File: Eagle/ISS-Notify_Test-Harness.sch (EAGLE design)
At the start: 36 parts, among them U1 ATMEGA32U4, U3 TPS63001, X1 8 MHz

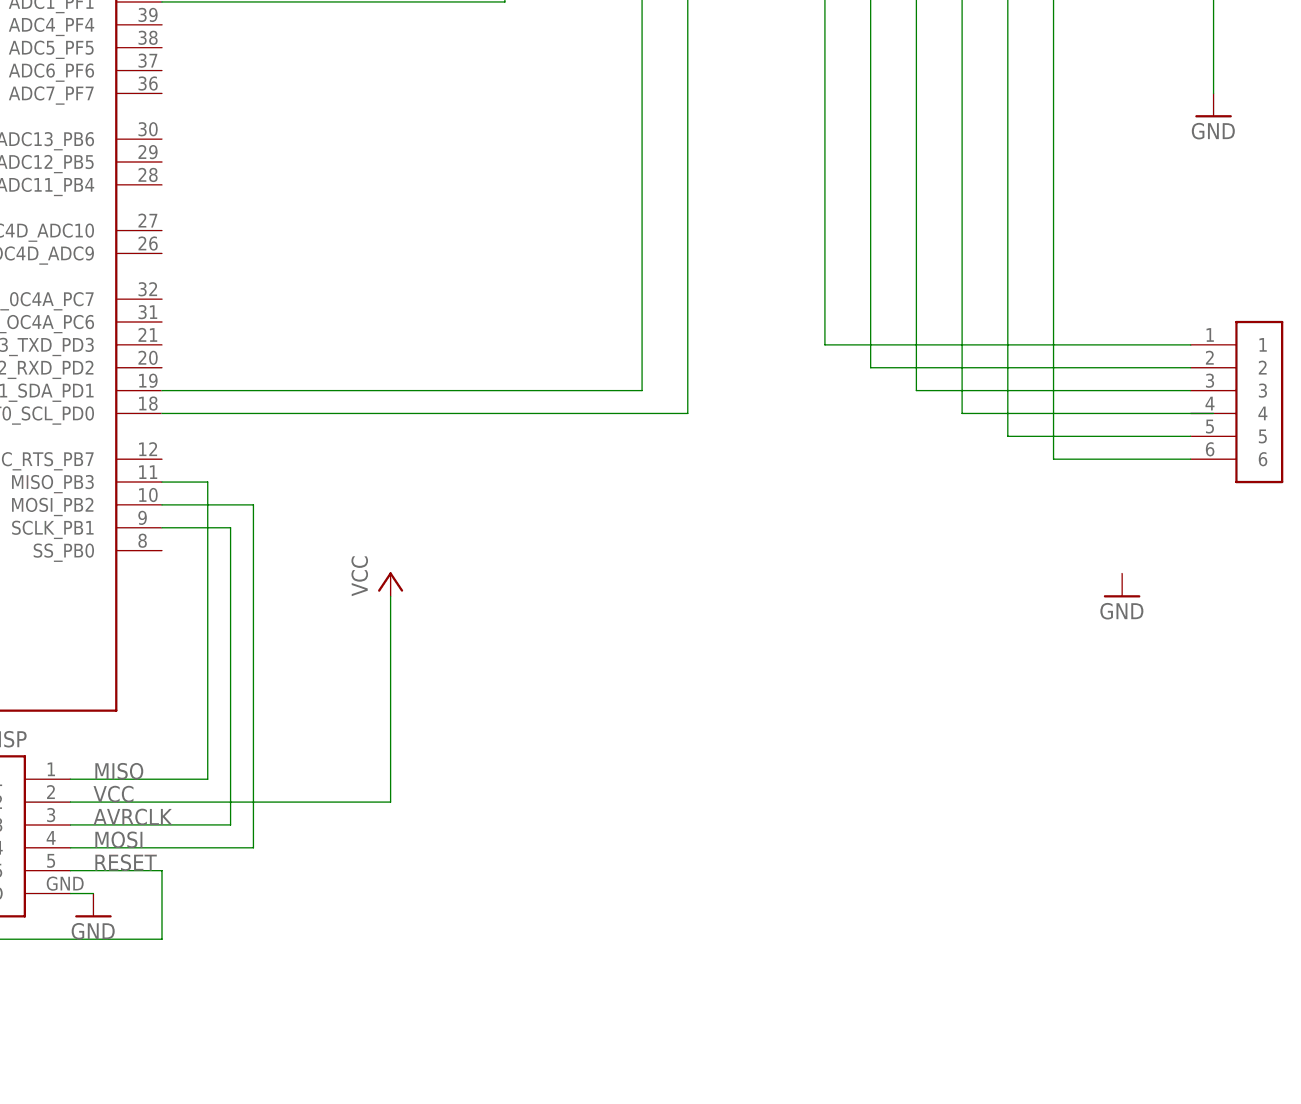
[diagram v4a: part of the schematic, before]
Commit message: 2 rgb status LEDs
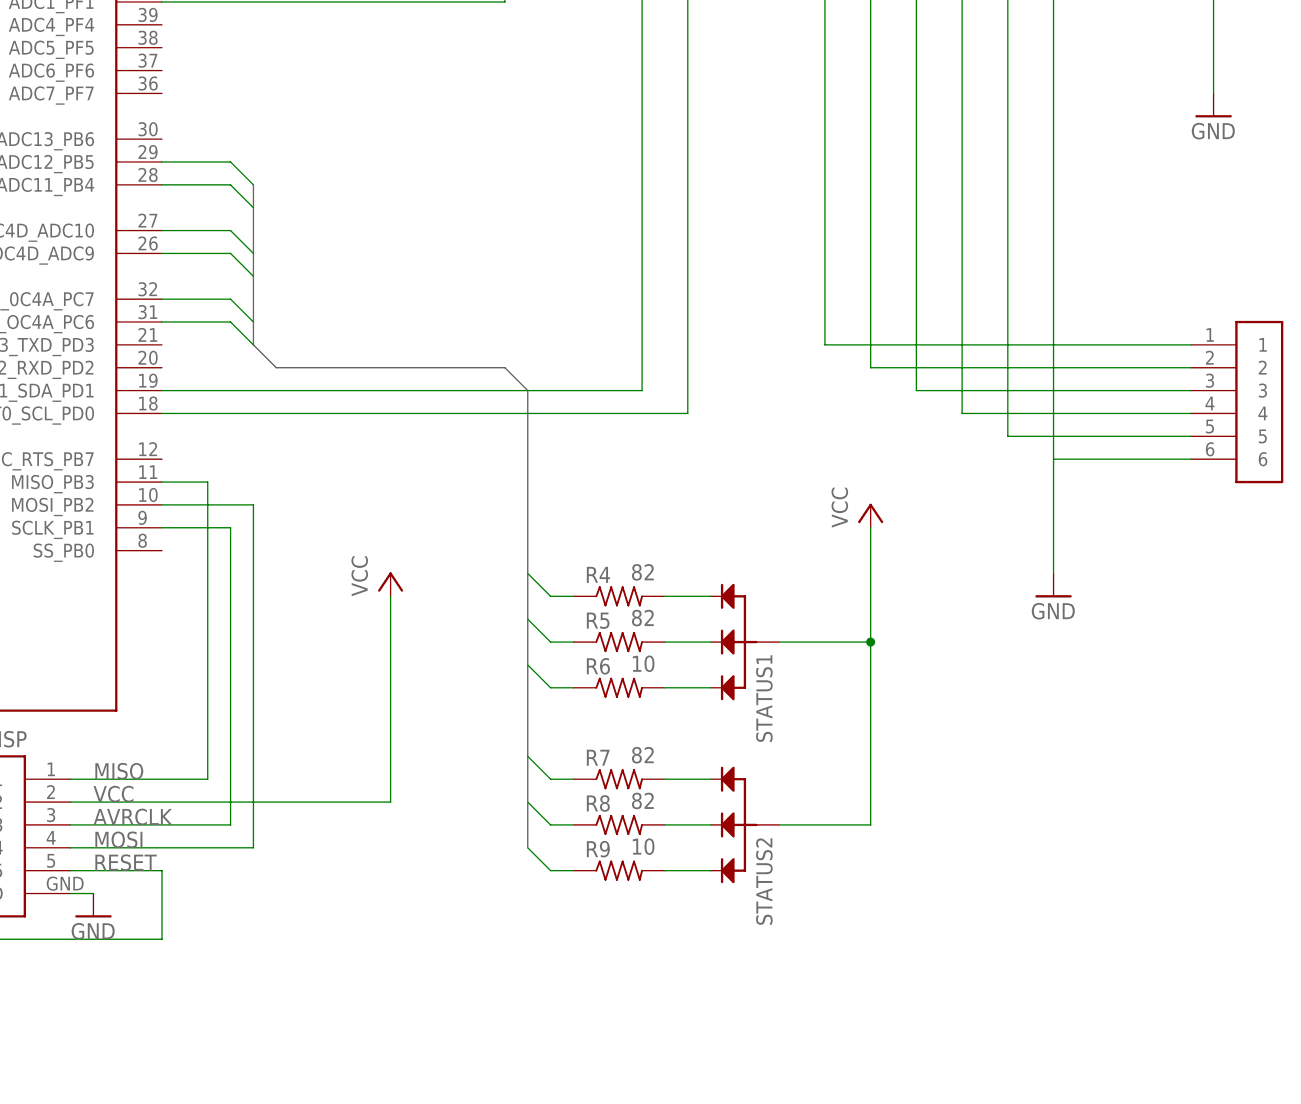
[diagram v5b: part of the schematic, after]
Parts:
- added R4, R5, R7, R8: 82, rcl_custom:R-US_0603-C-NOSILK
- added R6, R9: 10, rcl_custom:R-US_0603-C-NOSILK
- added STATUS1, STATUS2: RGBLED, ISS-Notify:RGBLED
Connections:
- removed net TESTGND: JPROGRAMER.6, TESTIGND.TEST
- new net LED1_B: R6.1, U1.T0_OC4D_ADC10
- new net LED1_G: R5.1, U1.ADC11_PB4
- new net LED1_R: R4.1, U1.OC1A_ADC12_PB5
- new net LED2_B: R9.1, U1.OC3A_OC4A_PC6
- new net LED2_G: R8.1, U1.ICP3_0C4A_PC7
- new net LED2_R: R7.1, U1.T1_OC4D_ADC9
- new net N$11: R8.2, STATUS2.G
- new net N$12: R9.2, STATUS2.B
- new net N$3: R4.2, STATUS1.R
- new net N$7: R5.2, STATUS1.G
- new net N$8: R6.2, STATUS1.B
- new net N$9: R7.2, STATUS2.R
- net GND: now also JPROGRAMER.6, TESTIGND.TEST
- net TESTMOSI: now also JPROGRAMER.4
- net VCC: now also STATUS1.ANODE, STATUS2.ANODE
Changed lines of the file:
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@@
 <part name="GND3" library="supply1" deviceset="GND" device=""/>
 <part name="JPROGRAMER" library="ISS-Notify" deviceset="6HEADER" device=""/>
+<part name="STATUS1" library="ISS-Notify" deviceset="RGBLED" device=""/>
+<part name="STATUS2" library="ISS-Notify" deviceset="RGBLED" device=""/>
+<part name="P+3" library="supply1" deviceset="VCC" device=""/>
+<part name="R4" library="rcl_custom" deviceset="R-US_" device="0603-C-NOSILK" value="82"/>
+<part name="R5" library="rcl_custom" deviceset="R-US_" device="0603-C-NOSILK" value="82"/>
+<part name="R6" library="rcl_custom" deviceset="R-US_" device="0603-C-NOSILK" value="10"/>
+<part name="R7" library="rcl_custom" deviceset="R-US_" device="0603-C-NOSILK" value="82"/>
+<part name="R8" library="rcl_custom" deviceset="R-US_" device="0603-C-NOSILK" value="82"/>
+<part name="R9" library="rcl_custom" deviceset="R-US_" device="0603-C-NOSILK" value="10"/>
 </parts>
 <sheets>
@@
 <instance part="TESTRESET" gate="G$1" x="322.58" y="198.12"/>
 <instance part="TESTIGND" gate="G$1" x="327.66" y="198.12"/>
-<instance part="GND3" gate="1" x="335.28" y="121.92"/>
+<instance part="GND3" gate="1" x="327.66" y="121.92"/>
 <instance part="JPROGRAMER" gate="G$1" x="350.52" y="144.78"/>
+<instance part="STATUS1" gate="G$1" x="292.1" y="116.84" rot="R270"/>
+<instance part="STATUS2" gate="G$1" x="292.1" y="96.52" rot="R270"/>
+<instance part="P+3" gate="VCC" x="307.34" y="132.08"/>
+<instance part="R4" gate="R" x="279.4" y="121.92" smashed="yes">
+<attribute name="NAME" x="275.59" y="123.4186" size="1.778" layer="95"/>
+<attribute name="VALUE" x="280.67" y="123.698" size="1.778" layer="96"/>
+</instance>
+<instance part="R5" gate="R" x="279.4" y="116.84" smashed="yes">
+<attribute name="NAME" x="275.59" y="118.3386" size="1.778" layer="95"/>
+<attribute name="VALUE" x="280.67" y="118.618" size="1.778" layer="96"/>
+</instance>
+<instance part="R6" gate="R" x="279.4" y="111.76" smashed="yes">
+<attribute name="NAME" x="275.59" y="113.2586" size="1.778" layer="95"/>
+<attribute name="VALUE" x="280.67" y="113.538" size="1.778" layer="96"/>
+</instance>
+<instance part="R7" gate="R" x="279.4" y="101.6" smashed="yes">
+<attribute name="NAME" x="275.59" y="103.0986" size="1.778" layer="95"/>
+<attribute name="VALUE" x="280.67" y="103.378" size="1.778" layer="96"/>
+</instance>
+<instance part="R8" gate="R" x="279.4" y="96.52" smashed="yes">
+<attribute name="NAME" x="275.59" y="98.0186" size="1.778" layer="95"/>
+<attribute name="VALUE" x="280.67" y="98.298" size="1.778" layer="96"/>
+</instance>
+<instance part="R9" gate="R" x="279.4" y="91.44" smashed="yes">
+<attribute name="NAME" x="275.59" y="92.9386" size="1.778" layer="95"/>
+<attribute name="VALUE" x="280.67" y="93.218" size="1.778" layer="96"/>
+</instance>
 </instances>
 <busses>
@@
 <wire x1="93.98" y1="109.22" x2="91.44" y2="106.68" width="0.762" layer="92"/>
 <wire x1="91.44" y1="106.68" x2="91.44" y2="96.52" width="0.762" layer="92"/>
+</segment>
+</bus>
+<bus name="LED1_R,LED1_G,LED1_B,LED2_R,LED2_G,LED2_B">
+<segment>
+<wire x1="269.24" y1="93.98" x2="269.24" y2="144.78" width="0.762" layer="92"/>
+<wire x1="269.24" y1="144.78" x2="266.7" y2="147.32" width="0.762" layer="92"/>
+<wire x1="266.7" y1="147.32" x2="241.3" y2="147.32" width="0.762" layer="92"/>
+<wire x1="241.3" y1="147.32" x2="238.76" y2="149.86" width="0.762" layer="92"/>
+<wire x1="238.76" y1="149.86" x2="238.76" y2="167.64" width="0.762" layer="92"/>
 </segment>
 </bus>
@@
 <pinref part="TESTGND" gate="G$1" pin="TEST"/>
 <wire x1="345.44" y1="177.8" x2="345.44" y2="198.12" width="0.1524" layer="91"/>
+</segment>
+<segment>
+<pinref part="JPROGRAMER" gate="G$1" pin="6"/>
+<pinref part="TESTIGND" gate="G$1" pin="TEST"/>
+<wire x1="342.9" y1="137.16" x2="327.66" y2="137.16" width="0.1524" layer="91"/>
+<wire x1="327.66" y1="137.16" x2="327.66" y2="198.12" width="0.1524" layer="91"/>
+<pinref part="GND3" gate="1" pin="GND"/>
+<wire x1="327.66" y1="137.16" x2="327.66" y2="124.46" width="0.1524" layer="91"/>
 </segment>
 </net>
@@
 <label x="220.98" y="99.06" size="1.778" layer="95"/>
 </segment>
+<segment>
+<pinref part="STATUS1" gate="G$1" pin="ANODE"/>
+<pinref part="P+3" gate="VCC" pin="VCC"/>
+<wire x1="297.18" y1="116.84" x2="307.34" y2="116.84" width="0.1524" layer="91"/>
+<wire x1="307.34" y1="116.84" x2="307.34" y2="129.54" width="0.1524" layer="91"/>
+<pinref part="STATUS2" gate="G$1" pin="ANODE"/>
+<wire x1="297.18" y1="96.52" x2="307.34" y2="96.52" width="0.1524" layer="91"/>
+<wire x1="307.34" y1="96.52" x2="307.34" y2="116.84" width="0.1524" layer="91"/>
+<junction x="307.34" y="116.84"/>
+</segment>
 </net>
 <net name="D-" class="0">
@@
 <segment>
 <pinref part="TESTMOSI" gate="G$1" pin="TEST"/>
-<wire x1="345.44" y1="142.24" x2="317.5" y2="142.24" width="0.1524" layer="91"/>
 <wire x1="317.5" y1="142.24" x2="317.5" y2="198.12" width="0.1524" layer="91"/>
+<pinref part="JPROGRAMER" gate="G$1" pin="4"/>
+<wire x1="342.9" y1="142.24" x2="317.5" y2="142.24" width="0.1524" layer="91"/>
 </segment>
 </net>
@@
 </segment>
 </net>
-<net name="TESTGND" class="0">
-<segment>
-<pinref part="JPROGRAMER" gate="G$1" pin="6"/>
-<pinref part="TESTIGND" gate="G$1" pin="TEST"/>
-<wire x1="342.9" y1="137.16" x2="327.66" y2="137.16" width="0.1524" layer="91"/>
-<wire x1="327.66" y1="137.16" x2="327.66" y2="198.12" width="0.1524" layer="91"/>
-</segment>
-</net>
+<net name="N$3" class="0">
+<segment>
+<pinref part="STATUS1" gate="G$1" pin="R"/>
+<pinref part="R4" gate="R" pin="2"/>
+<wire x1="284.48" y1="121.92" x2="289.56" y2="121.92" width="0.1524" layer="91"/>
+</segment>
+</net>
+<net name="N$7" class="0">
+<segment>
+<pinref part="STATUS1" gate="G$1" pin="G"/>
+<pinref part="R5" gate="R" pin="2"/>
+<wire x1="289.56" y1="116.84" x2="284.48" y2="116.84" width="0.1524" layer="91"/>
+</segment>
+</net>
+<net name="N$8" class="0">
+<segment>
+<pinref part="STATUS1" gate="G$1" pin="B"/>
+<pinref part="R6" gate="R" pin="2"/>
+<wire x1="289.56" y1="111.76" x2="284.48" y2="111.76" width="0.1524" layer="91"/>
+</segment>
+</net>
+<net name="N$9" class="0">
+<segment>
+<pinref part="STATUS2" gate="G$1" pin="R"/>
+<pinref part="R7" gate="R" pin="2"/>
+<wire x1="289.56" y1="101.6" x2="284.48" y2="101.6" width="0.1524" layer="91"/>
+</segment>
+</net>
+<net name="N$11" class="0">
+<segment>
+<pinref part="STATUS2" gate="G$1" pin="G"/>
+<pinref part="R8" gate="R" pin="2"/>
+<wire x1="289.56" y1="96.52" x2="284.48" y2="96.52" width="0.1524" layer="91"/>
+</segment>
+</net>
+<net name="N$12" class="0">
+<segment>
+<pinref part="STATUS2" gate="G$1" pin="B"/>
+<pinref part="R9" gate="R" pin="2"/>
+<wire x1="289.56" y1="91.44" x2="284.48" y2="91.44" width="0.1524" layer="91"/>
+</segment>
+</net>
+<net name="LED2_B" class="0">
+<segment>
+<wire x1="269.24" y1="93.98" x2="271.78" y2="91.44" width="0.1524" layer="91"/>
+<pinref part="R9" gate="R" pin="1"/>
+<wire x1="271.78" y1="91.44" x2="274.32" y2="91.44" width="0.1524" layer="91"/>
+</segment>
+<segment>
+<wire x1="238.76" y1="149.86" x2="236.22" y2="152.4" width="0.1524" layer="91"/>
+<wire x1="236.22" y1="152.4" x2="228.6" y2="152.4" width="0.1524" layer="91"/>
+<pinref part="U1" gate="ATMEGA" pin="OC3A_OC4A_PC6"/>
+</segment>
+</net>
+<net name="LED2_G" class="0">
+<segment>
+<wire x1="269.24" y1="99.06" x2="271.78" y2="96.52" width="0.1524" layer="91"/>
+<pinref part="R8" gate="R" pin="1"/>
+<wire x1="274.32" y1="96.52" x2="271.78" y2="96.52" width="0.1524" layer="91"/>
+</segment>
+<segment>
+<wire x1="238.76" y1="152.4" x2="236.22" y2="154.94" width="0.1524" layer="91"/>
+<pinref part="U1" gate="ATMEGA" pin="ICP3_0C4A_PC7"/>
+<wire x1="236.22" y1="154.94" x2="228.6" y2="154.94" width="0.1524" layer="91"/>
+</segment>
+</net>
+<net name="LED2_R" class="0">
+<segment>
+<wire x1="269.24" y1="104.14" x2="271.78" y2="101.6" width="0.1524" layer="91"/>
+<pinref part="R7" gate="R" pin="1"/>
+<wire x1="274.32" y1="101.6" x2="271.78" y2="101.6" width="0.1524" layer="91"/>
+</segment>
+<segment>
+<wire x1="238.76" y1="157.48" x2="236.22" y2="160.02" width="0.1524" layer="91"/>
+<pinref part="U1" gate="ATMEGA" pin="T1_OC4D_ADC9"/>
+<wire x1="236.22" y1="160.02" x2="228.6" y2="160.02" width="0.1524" layer="91"/>
+</segment>
+</net>
+<net name="LED1_B" class="0">
+<segment>
+<wire x1="269.24" y1="114.3" x2="271.78" y2="111.76" width="0.1524" layer="91"/>
+<pinref part="R6" gate="R" pin="1"/>
+<wire x1="271.78" y1="111.76" x2="274.32" y2="111.76" width="0.1524" layer="91"/>
+</segment>
+<segment>
+<wire x1="238.76" y1="160.02" x2="236.22" y2="162.56" width="0.1524" layer="91"/>
+<pinref part="U1" gate="ATMEGA" pin="T0_OC4D_ADC10"/>
+<wire x1="236.22" y1="162.56" x2="228.6" y2="162.56" width="0.1524" layer="91"/>
+</segment>
+</net>
+<net name="LED1_G" class="0">
+<segment>
+<wire x1="269.24" y1="119.38" x2="271.78" y2="116.84" width="0.1524" layer="91"/>
+<pinref part="R5" gate="R" pin="1"/>
+<wire x1="271.78" y1="116.84" x2="274.32" y2="116.84" width="0.1524" layer="91"/>
+</segment>
+<segment>
+<wire x1="238.76" y1="165.1" x2="236.22" y2="167.64" width="0.1524" layer="91"/>
+<pinref part="U1" gate="ATMEGA" pin="ADC11_PB4"/>
+<wire x1="236.22" y1="167.64" x2="228.6" y2="167.64" width="0.1524" layer="91"/>
+</segment>
+</net>
+<net name="LED1_R" class="0">
+<segment>
+<wire x1="269.24" y1="124.46" x2="271.78" y2="121.92" width="0.1524" layer="91"/>
+<pinref part="R4" gate="R" pin="1"/>
+<wire x1="271.78" y1="121.92" x2="274.32" y2="121.92" width="0.1524" layer="91"/>
+</segment>
+<segment>
+<wire x1="238.76" y1="167.64" x2="236.22" y2="170.18" width="0.1524" layer="91"/>
+<pinref part="U1" gate="ATMEGA" pin="OC1A_ADC12_PB5"/>
+<wire x1="236.22" y1="170.18" x2="228.6" y2="170.18" width="0.1524" layer="91"/>
+</segment>
+</net>

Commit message: route status LEDs
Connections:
- net LED1_B: now also U1.OC1A_ADC12_PB5; no longer U1.T0_OC4D_ADC10
- net LED1_G: now also U1.ICP3_0C4A_PC7; no longer U1.ADC11_PB4
- net LED1_R: now also U1.OC3A_OC4A_PC6; no longer U1.OC1A_ADC12_PB5
- net LED2_B: now also U1.T1_OC4D_ADC9; no longer U1.OC3A_OC4A_PC6
- net LED2_G: now also U1.ADC11_PB4; no longer U1.ICP3_0C4A_PC7
- net LED2_R: now also U1.T0_OC4D_ADC10; no longer U1.T1_OC4D_ADC9
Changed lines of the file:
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@@
 </segment>
 <segment>
-<wire x1="238.76" y1="149.86" x2="236.22" y2="152.4" width="0.1524" layer="91"/>
-<wire x1="236.22" y1="152.4" x2="228.6" y2="152.4" width="0.1524" layer="91"/>
-<pinref part="U1" gate="ATMEGA" pin="OC3A_OC4A_PC6"/>
+<wire x1="238.76" y1="157.48" x2="236.22" y2="160.02" width="0.1524" layer="91"/>
+<pinref part="U1" gate="ATMEGA" pin="T1_OC4D_ADC9"/>
+<wire x1="236.22" y1="160.02" x2="228.6" y2="160.02" width="0.1524" layer="91"/>
 </segment>
 </net>
@@
 </segment>
 <segment>
-<wire x1="238.76" y1="152.4" x2="236.22" y2="154.94" width="0.1524" layer="91"/>
-<pinref part="U1" gate="ATMEGA" pin="ICP3_0C4A_PC7"/>
-<wire x1="236.22" y1="154.94" x2="228.6" y2="154.94" width="0.1524" layer="91"/>
+<wire x1="238.76" y1="165.1" x2="236.22" y2="167.64" width="0.1524" layer="91"/>
+<pinref part="U1" gate="ATMEGA" pin="ADC11_PB4"/>
+<wire x1="236.22" y1="167.64" x2="228.6" y2="167.64" width="0.1524" layer="91"/>
 </segment>
 </net>
@@
 </segment>
 <segment>
-<wire x1="238.76" y1="157.48" x2="236.22" y2="160.02" width="0.1524" layer="91"/>
-<pinref part="U1" gate="ATMEGA" pin="T1_OC4D_ADC9"/>
-<wire x1="236.22" y1="160.02" x2="228.6" y2="160.02" width="0.1524" layer="91"/>
+<wire x1="238.76" y1="160.02" x2="236.22" y2="162.56" width="0.1524" layer="91"/>
+<pinref part="U1" gate="ATMEGA" pin="T0_OC4D_ADC10"/>
+<wire x1="236.22" y1="162.56" x2="228.6" y2="162.56" width="0.1524" layer="91"/>
 </segment>
 </net>
@@
 </segment>
 <segment>
-<wire x1="238.76" y1="160.02" x2="236.22" y2="162.56" width="0.1524" layer="91"/>
-<pinref part="U1" gate="ATMEGA" pin="T0_OC4D_ADC10"/>
-<wire x1="236.22" y1="162.56" x2="228.6" y2="162.56" width="0.1524" layer="91"/>
+<wire x1="238.76" y1="167.64" x2="236.22" y2="170.18" width="0.1524" layer="91"/>
+<pinref part="U1" gate="ATMEGA" pin="OC1A_ADC12_PB5"/>
+<wire x1="236.22" y1="170.18" x2="228.6" y2="170.18" width="0.1524" layer="91"/>
 </segment>
 </net>
@@
 </segment>
 <segment>
-<wire x1="238.76" y1="165.1" x2="236.22" y2="167.64" width="0.1524" layer="91"/>
-<pinref part="U1" gate="ATMEGA" pin="ADC11_PB4"/>
-<wire x1="236.22" y1="167.64" x2="228.6" y2="167.64" width="0.1524" layer="91"/>
+<wire x1="238.76" y1="152.4" x2="236.22" y2="154.94" width="0.1524" layer="91"/>
+<pinref part="U1" gate="ATMEGA" pin="ICP3_0C4A_PC7"/>
+<wire x1="236.22" y1="154.94" x2="228.6" y2="154.94" width="0.1524" layer="91"/>
 </segment>
 </net>
@@
 </segment>
 <segment>
-<wire x1="238.76" y1="167.64" x2="236.22" y2="170.18" width="0.1524" layer="91"/>
-<pinref part="U1" gate="ATMEGA" pin="OC1A_ADC12_PB5"/>
-<wire x1="236.22" y1="170.18" x2="228.6" y2="170.18" width="0.1524" layer="91"/>
+<wire x1="238.76" y1="149.86" x2="236.22" y2="152.4" width="0.1524" layer="91"/>
+<pinref part="U1" gate="ATMEGA" pin="OC3A_OC4A_PC6"/>
+<wire x1="236.22" y1="152.4" x2="228.6" y2="152.4" width="0.1524" layer="91"/>
 </segment>
 </net>

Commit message: move power supply over a little
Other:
- moved on the sheet: AVRISP, C1, C10, C12, C13, C2, C3, C4, C5, C6, L1, R1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

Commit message: Added LTC1153 package to library. Added to schematic without circuit. Needs another look in the morning.
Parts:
- removed USB: CON_USB-MICRO-6GND, ISS-Notify:CON_USB-MICRO-6GND
- added J1: CON_USB-MICRO-ZX62D-B-5P8, ISS-Notify:CON_USB-MICRO-ZX62D-B-5P8
- added Q1: NTR4501N-D, max-viz:NTR4501N-D
- added U2: LTC1153CS8, ISS-Notify:LTC1153CS8
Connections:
- new net N$13: U1.PE6_ANIO_INT6
- net GND: now also J1.GND, J1.SHLD@1, J1.SHLD@2, J1.SHLD@3, J1.SHLD@4; no longer USB.5
- net N$4: now also J1.D+; no longer USB.3
- net N$5: now also J1.D-; no longer USB.2
- net TESTVCC: now also TESTVBAT.TEST
- net VCC: now also Q1.D
- net VIN: now also J1.VCC; no longer USB.1
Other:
- note added: "3.3V"
- note added: "5V"
- note added: "PUT A SHORT DETECTION IN HERE THAT OPENS THE MOSFET TO SAVE THE CIRCUIT AND THEN REPORTS BACK TO THE MICROCONTROLLER"
- moved on the sheet: TESTGND, TESTVBAT
